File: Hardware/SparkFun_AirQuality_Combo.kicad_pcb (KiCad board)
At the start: 2 copper layers, 82.6 x 44.5 mm, 57 parts, among them J1 Qwiic_RA, J2 Qwiic_RA, J3 Conn_01x04, U1 SEN55, U3 SCD41, U4 SEN55_Outline, U5 AP3012

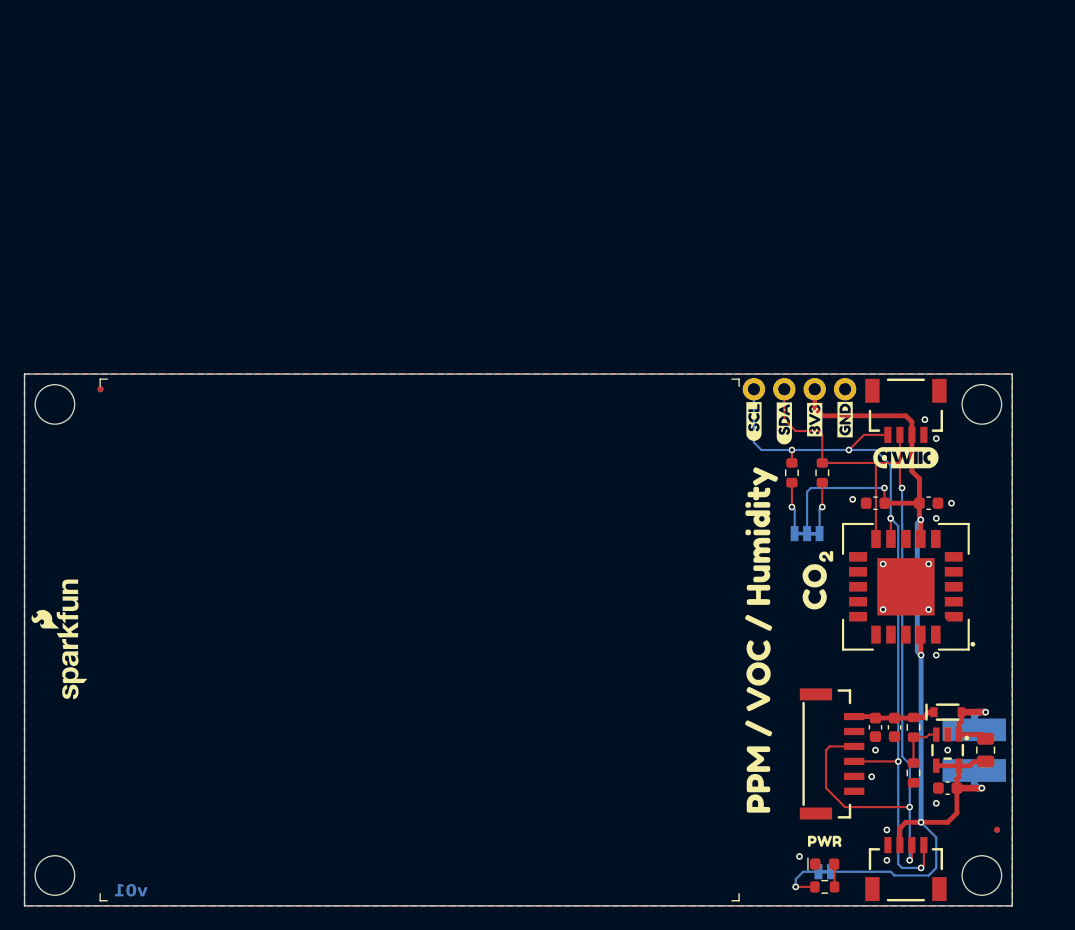
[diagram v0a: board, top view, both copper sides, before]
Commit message: Move connector to avoid cable over silk
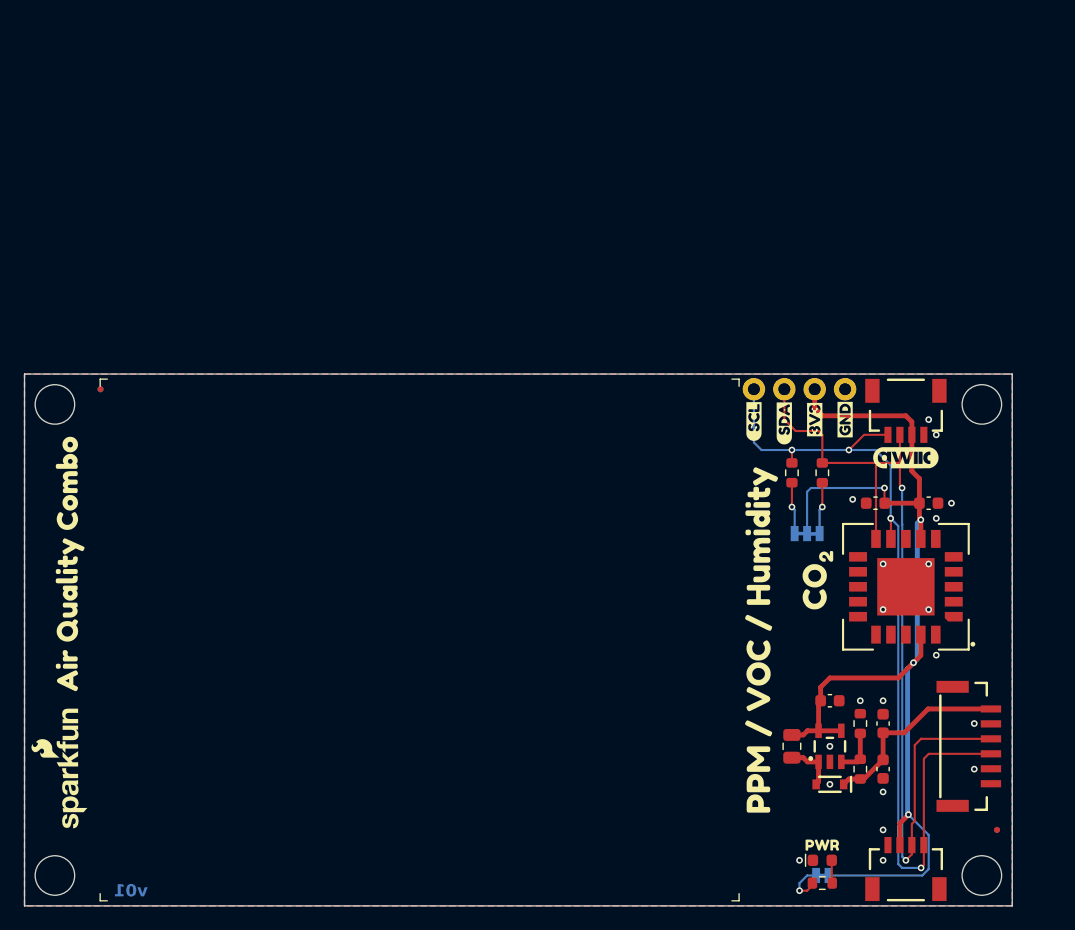
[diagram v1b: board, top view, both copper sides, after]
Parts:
- removed C3: 4.7uF, SparkFun-Capacitor:C_0603_1608Metric
- removed G1: OSHW_Logo, SparkFun-Aesthetic:Creative_Commons_License
- removed L1: 10uH_5x5mm_1.0A, SparkFun-Coil:INDUCTOR_4.7X4.7MM
- added C1: 22uF, SparkFun-Capacitor:C_0603_1608Metric, F.Cu at (173.4, 141.0)
- added G4: OSHW_Logo, SparkFun-Aesthetic:Creative_Commons_License, F.Cu at (108.0, 163.8)
- added kibuzzard-65CFEE26: G***, kibuzzard-65CFEE26, F.Cu at (105.4, 123.8)
- C4: value 0.1uF -> 4.7uF
- C5: value 22uF -> 0.1uF
- D2: value 0.5A -> PMEG4005EJ
- FID1, FID2, FID3, FID4: value Fiducial_0.5 -> Fiducial_0.5mm
- J1, J2: footprint SparkFun-Connector:JST04_1MM_RA -> SparkFun-Connector:JST_SMD_1.0mm-4_RA
- J3: footprint SparkFun-Connector:1X04 -> SparkFun-Connector:1x04
- JP1: footprint SparkFun-Jumper:SMT-JUMPER_3_2-NC_TRACE_SILK -> SparkFun-Jumper:Jumper_2_NC_Trace
- JP2: footprint SparkFun-Jumper:SMT-JUMPER_2_NC_TRACE_SILK -> SparkFun-Jumper:Jumper_3_NC-2_Trace
- ST1, ST2, ST3, ST4: value Stand_off -> Standoff; footprint SparkFun-Hardware:STAND-OFF -> SparkFun-Hardware:Standoff
- U1: footprint SparkFun-Connector:JST-6-SMD-1.25MM-LOCKING -> SparkFun-Connector:JST_SMD_1.25mm-6_Locking
- U4: footprint SparkFun-Sensor:SEN5x-Outline -> SparkFun-Sensor:SEN5x_Outline
- U7: footprint SparkFun-Aesthetic:ORDERING_INSTRUCTIONS -> SparkFun-Aesthetic:Ordering_Instructions
- moved JP1 28.6 mm to (168.3, 149.9)
- moved JP2 28.3 mm to (167.0, 121.3)
- moved C5 18.7 mm to (172.7, 118.7), turned to 180 degrees
- moved L2 16.2 mm to (165.7, 139.1), turned to -90 degrees
- moved C7 12.3 mm to (168.9, 135.3), turned to 0 degrees
- moved D2 11.5 mm to (168.9, 142.2), turned to 180 degrees
- moved U1 11.4 mm to (179.1, 139.1)
- moved G*** 10.8 mm to (105.4, 141.0)
- moved U5 9.85 mm to (168.9, 139.1), turned to 90 degrees
- moved R6 6.07 mm to (171.4, 137.2), turned to 90 degrees
- moved R5 5.65 mm to (171.4, 141.0), turned to 90 degrees
- moved C9 1.00 mm to (173.4, 137.2), turned to 90 degrees
- moved kibuzzard-65A8AED7 0.46 mm to (165.1, 149.9)
- moved D1 0.38 mm to (168.3, 148.6)
- moved R3 0.38 mm to (168.3, 150.5)
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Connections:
- C5 pad 1: 5V -> 3.3V
- R1 pad 1: Net-(JP1-B) -> Net-(JP2-B)
- R2 pad 1: Net-(JP1-A) -> Net-(JP2-A)
- R3 pad 1: Net-(JP2-A) -> Net-(JP1-A)
- U1 pad NC1: (no net) -> unconnected-(U1-NC-PadNC1)
- U1 pad NC2: (no net) -> unconnected-(U1-NC-PadNC2)
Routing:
- net 5V: track 6.92 -> 16.2 mm
- net SCL: track 64.6 -> 73.9 mm, vias 5 -> 4
- net Net-(JP2-B): track 0.00 -> 4.35 mm, vias 0 -> 1
- net Net-(JP1-B): track 4.35 -> 0.00 mm, vias 1 -> 0
- net Net-(U5-SW): track 8.59 -> 4.33 mm, vias 1 -> 0
- net SDA: track 72.0 -> 73.7 mm, vias 3 -> 2
- net 3.3V: track 94.3 -> 95.5 mm, vias 5 -> 4
- net Net-(JP1-A): track 4.35 -> 3.74 mm
- net GND: vias 17 -> 20

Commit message: Pre design review changes
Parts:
- removed U7: ~, SparkFun-Aesthetic:Ordering_Instructions
- added C2: 22uF, SparkFun-Capacitor:C_0805_2012Metric, F.Cu at (176.5, 111.8)
- C1: value 22uF -> 0.1uF
- moved G4 106.8 mm to (214.6, 168.9)
- moved C1 38.7 mm to (180.3, 102.9), turned to 0 degrees
- moved C4 29.4 mm to (180.3, 89.5)
- moved C5 29.4 mm to (175.9, 89.5)
- moved D1 29.4 mm to (171.4, 119.4)
- moved D2 29.4 mm to (172.1, 113.0)
- moved FID1 29.4 mm to (186.1, 116.8)
- moved FID4 29.4 mm to (186.1, 116.8)
- moved G*** 29.4 mm to (178.4, 85.7)
- moved J2 29.4 mm to (178.4, 83.8)
- moved JP1 29.4 mm to (171.4, 120.7)
- moved R3 29.4 mm to (171.4, 121.3)
- moved ST2 29.4 mm to (184.8, 120.7)
- moved ST4 29.4 mm to (107.3, 120.7)
- moved U3 29.4 mm to (178.4, 96.5)
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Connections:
- C1 pad 1: 5V -> 3.3V
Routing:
- net 3.3V: track 95.5 -> 89.7 mm, vias 4 -> 5
- net GND: vias 20 -> 31
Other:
- board size 82.6 x 44.5 mm -> 82.5 x 44.5 mm
- board text added: "Ordering Notes"
- board text added: "Outer Copper Weight: 1oz"
- board text added: "Silkscreen Color: White"
- board text added: "v10"
- board text removed: "Copper Weight: 1oz"
- board text removed: "N. Seidle"
- board text removed: "v01"

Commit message: Add PTH at 0.8"
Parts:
- removed kibuzzard-65A75D38: G***, kibuzzard-65A75D38
- removed kibuzzard-65A75DA3: G***, kibuzzard-65A75DA3
- added ST5: Standoff, SparkFun-Hardware:Standoff, F.Cu at (184.8, 100.3)
- added TP1: 0.75mm, SparkFun-Connector:TestPoint-0.75mm, B.Cu at (174.6, 115.6)
- added U2: ~, SparkFun-Aesthetic:Ordering_Instructions, F.Cu at (198.8, 75.0)
- added kibuzzard-65F20621: G***, kibuzzard-65F20621, F.Cu at (166.1, 104.8)
- moved kibuzzard-65A75D7A 8.99 mm to (167.0, 86.4)
- moved C5 2.54 mm to (173.4, 89.5)
- moved C1 2.54 mm to (177.8, 102.9)
- moved C4 2.54 mm to (177.8, 89.5)
- moved U3 2.54 mm to (175.9, 96.5)
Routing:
- net 5V: track 16.2 -> 19.2 mm, vias 0 -> 1
- net 3.3V: track 89.7 -> 92.2 mm
- net SCL: track 73.5 -> 72.9 mm
- net GND: vias 31 -> 32
